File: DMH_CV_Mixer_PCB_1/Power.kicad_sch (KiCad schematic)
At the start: 14 parts, among them J0 Conn_01x01, J100 IDC_02x05, J101 IDC_02x08

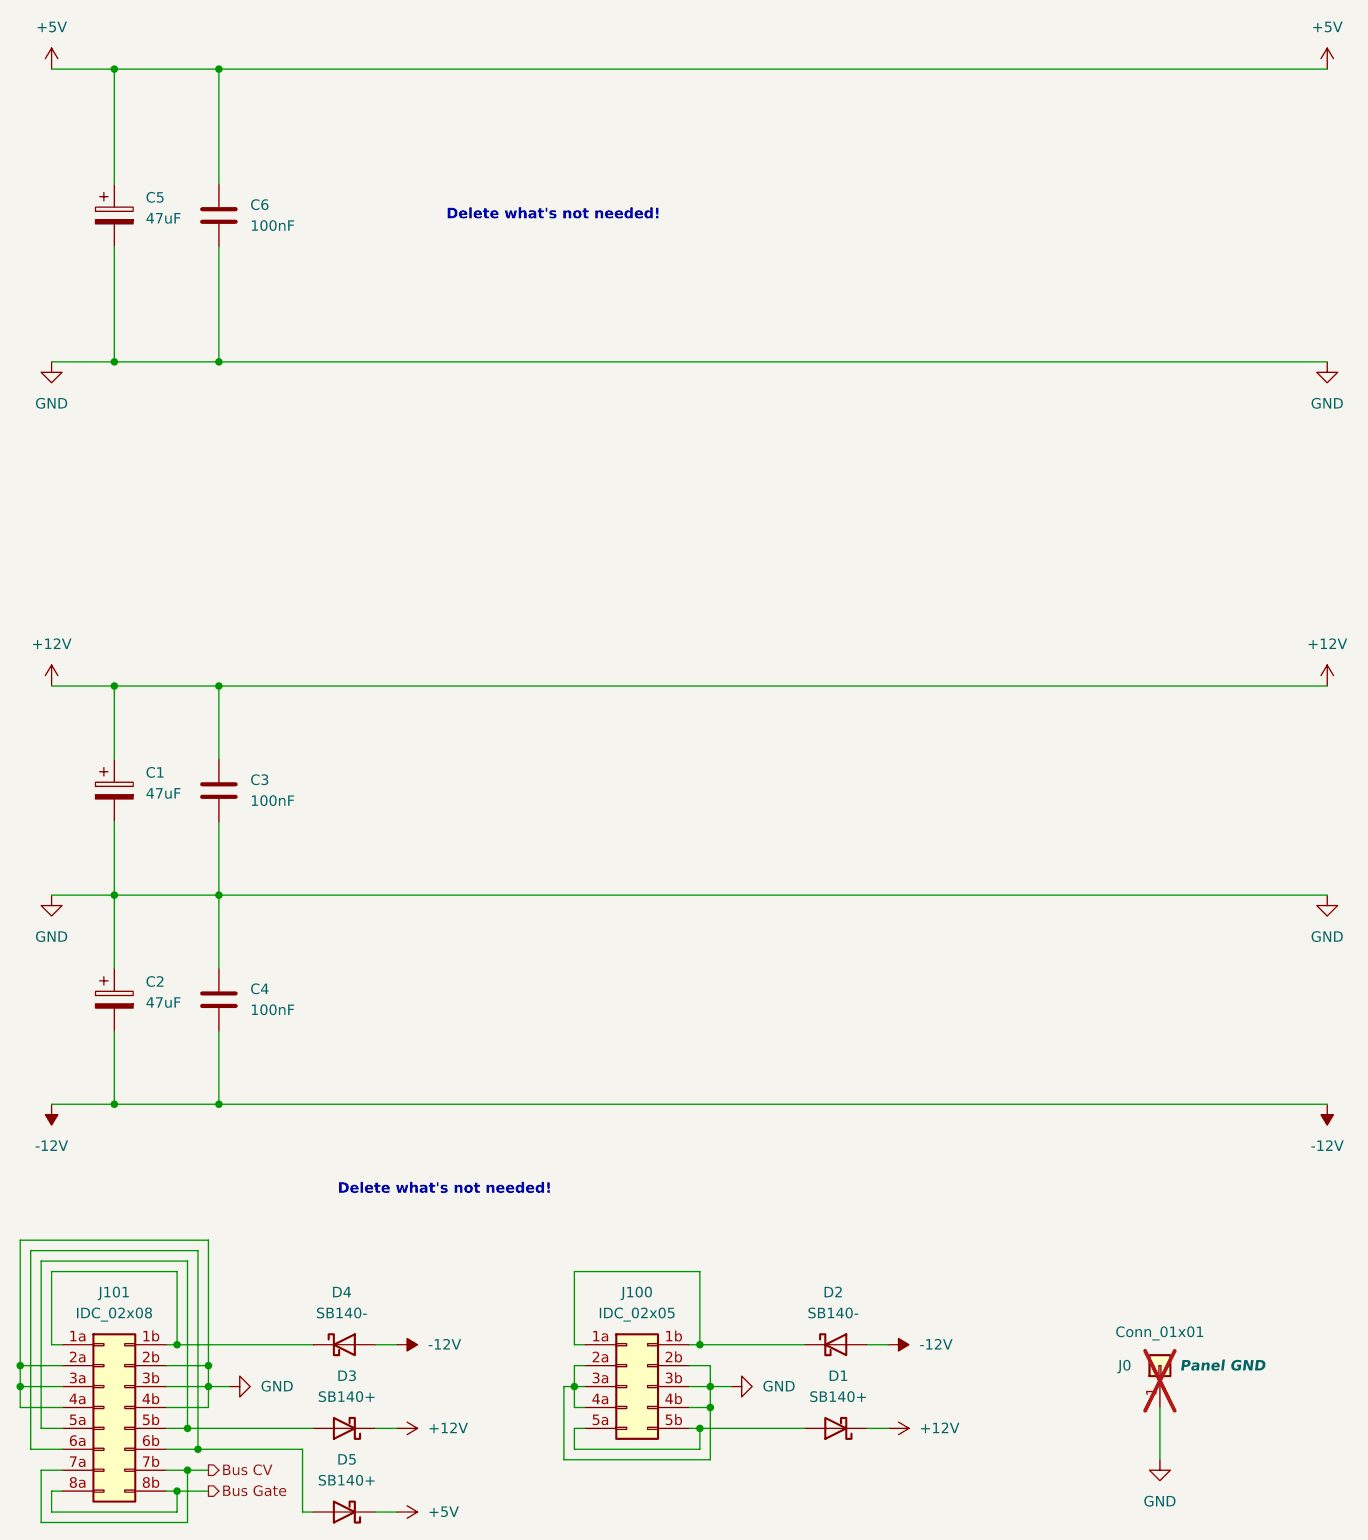
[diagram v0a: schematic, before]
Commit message: Started IO part design
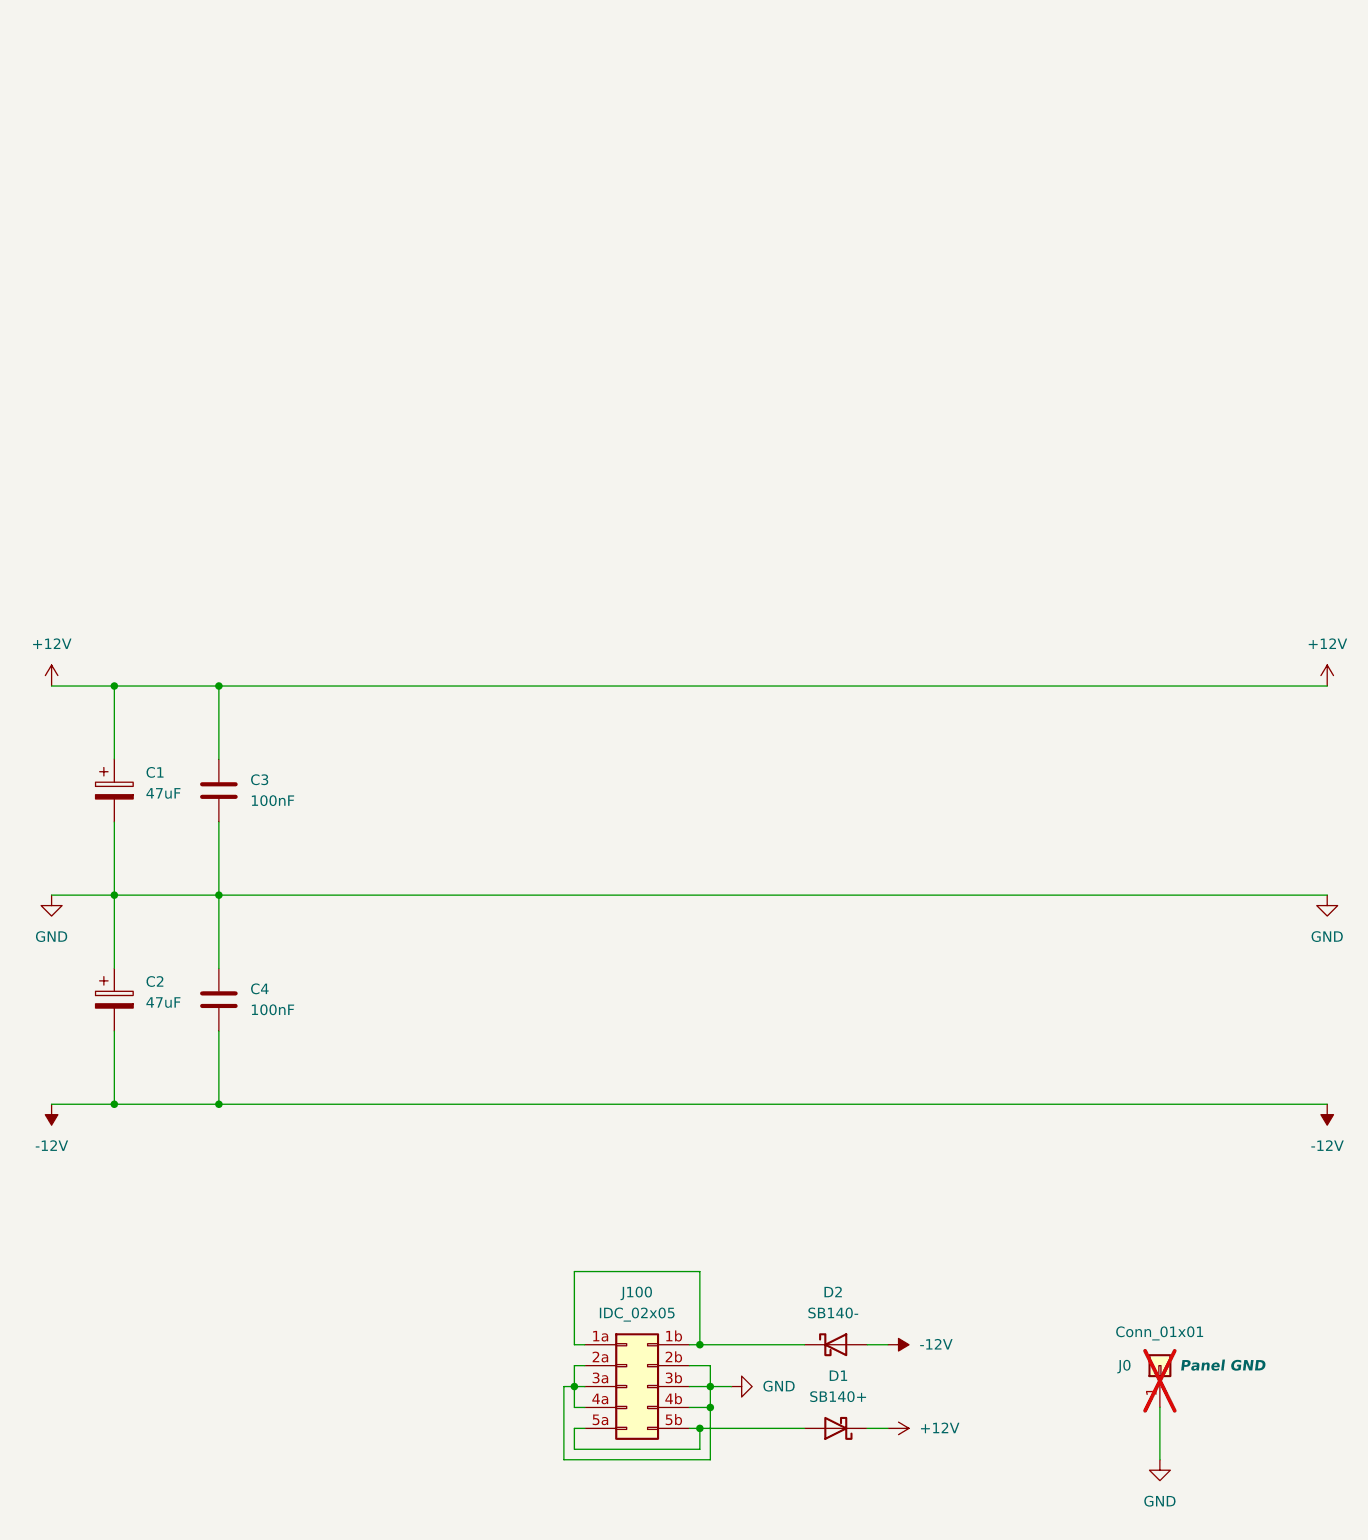
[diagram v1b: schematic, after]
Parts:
- removed C5: 47uF, Capacitor_THT:CP_Radial_D4.0mm_P1.50mm, symbol Device:C_Polarized
- removed C6: 100nF, Capacitor_THT:C_Disc_D4.3mm_W1.9mm_P5.00mm, symbol Device:C
- removed D3, D5: SB140+, Diode_THT:D_DO-41_SOD81_P10.16mm_Horizontal, symbol SynthStuff:Power_Bus_Schotty_+
- removed D4: SB140-, Diode_THT:D_DO-41_SOD81_P10.16mm_Horizontal, symbol SynthStuff:Power_Bus_Schotty_-
- removed J101: IDC_02x08, SynthStuff:IDC-Header_2x08_P2.54mm_Vertical_Eurorack, symbol SynthStuff:Eurorack_Power_Connector_16Pin
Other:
- note removed: "Delete what's not needed!"
